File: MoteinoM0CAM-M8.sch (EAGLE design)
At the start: 17 parts

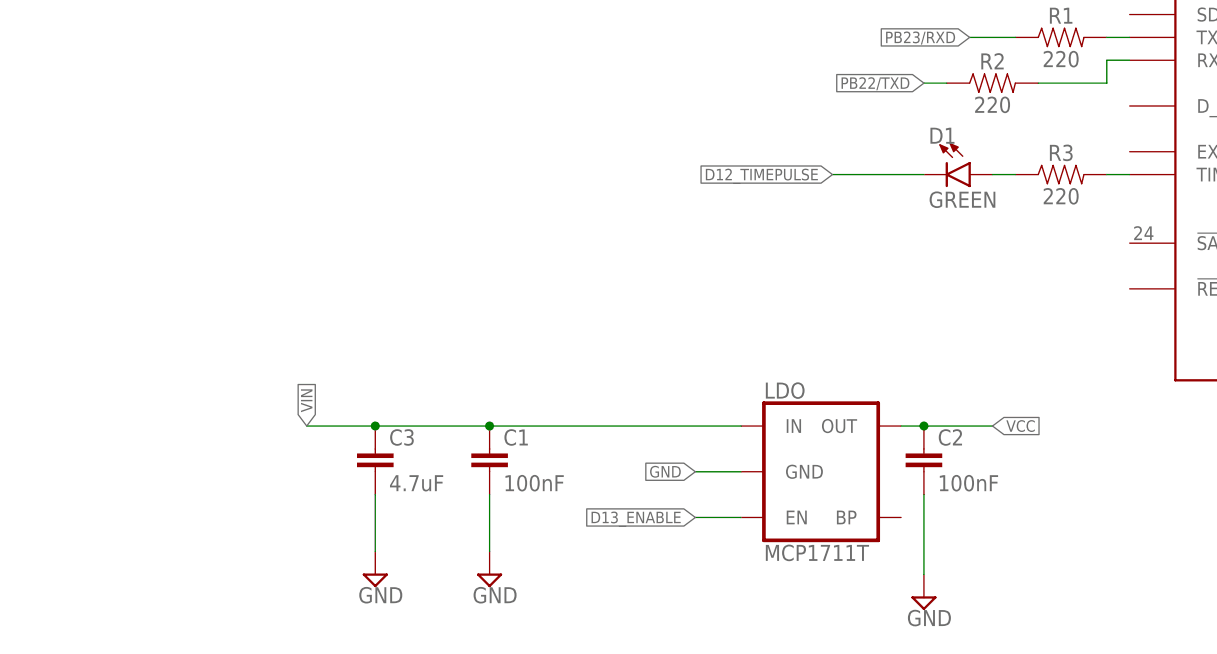
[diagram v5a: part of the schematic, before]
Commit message: moved 4.7uF
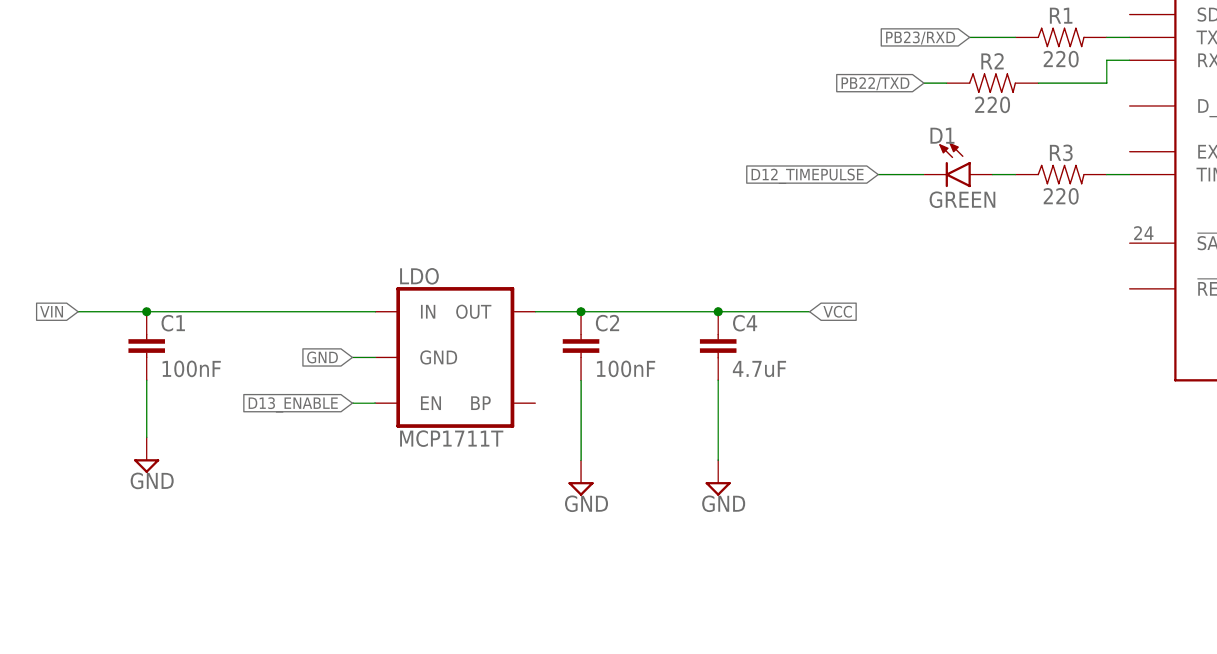
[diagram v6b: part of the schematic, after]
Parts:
- removed C3: 4.7uF, SparkFun-Capacitors:4.7UF0603
- added C4: 4.7uF, SparkFun-Capacitors:4.7UF0603
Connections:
- net GND: now also C4.2; no longer C3.2
- net VCC: now also C4.1
- net VIN: no longer C3.1
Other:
- moved on the sheet: C1, C2, LDO
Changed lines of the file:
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@@
 <part name="R2" library="SparkFun-Resistors" library_urn="urn:adsk.eagle:library:532" deviceset="220OHM" device="-0603-1/10W-1%" package3d_urn="urn:adsk.eagle:package:39650/1" value="220"/>
 <part name="R3" library="SparkFun-Resistors" library_urn="urn:adsk.eagle:library:532" deviceset="220OHM" device="-0603-1/10W-1%" package3d_urn="urn:adsk.eagle:package:39650/1" value="220"/>
-<part name="C3" library="SparkFun-Capacitors" library_urn="urn:adsk.eagle:library:510" deviceset="4.7UF" device="0603" package3d_urn="urn:adsk.eagle:package:37414/1" value="4.7uF"/>
-<part name="SUPPLY4" library="supply2" library_urn="urn:adsk.eagle:library:372" deviceset="GND" device=""/>
+<part name="C4" library="SparkFun-Capacitors" library_urn="urn:adsk.eagle:library:510" deviceset="4.7UF" device="0603" package3d_urn="urn:adsk.eagle:package:37414/1" value="4.7uF"/>
+<part name="SUPPLY5" library="supply2" library_urn="urn:adsk.eagle:library:372" deviceset="GND" device=""/>
 </parts>
 <sheets>
@@
 <attribute name="VALUE" x="47.752" y="162.814" size="1.778" layer="96" font="vector"/>
 </instance>
-<instance part="LDO" gate="G$1" x="55.88" y="106.68" smashed="yes">
-<attribute name="NAME" x="48.26" y="114.808" size="1.778" layer="95" font="vector"/>
-<attribute name="VALUE" x="48.26" y="98.552" size="1.778" layer="96" font="vector" align="top-left"/>
-</instance>
-<instance part="C1" gate="G$1" x="17.78" y="106.68" smashed="yes">
-<attribute name="NAME" x="19.304" y="109.601" size="1.778" layer="95" font="vector"/>
-<attribute name="VALUE" x="19.304" y="104.521" size="1.778" layer="96" font="vector"/>
-</instance>
-<instance part="C2" gate="G$1" x="66.04" y="106.68" smashed="yes">
-<attribute name="NAME" x="67.564" y="109.601" size="1.778" layer="95" font="vector"/>
-<attribute name="VALUE" x="67.564" y="104.521" size="1.778" layer="96" font="vector"/>
-</instance>
-<instance part="SUPPLY2" gate="GND" x="17.78" y="95.25" smashed="yes">
-<attribute name="VALUE" x="15.875" y="92.075" size="1.778" layer="96"/>
-</instance>
-<instance part="SUPPLY3" gate="GND" x="66.04" y="92.71" smashed="yes">
-<attribute name="VALUE" x="64.135" y="89.535" size="1.778" layer="96"/>
+<instance part="LDO" gate="G$1" x="15.24" y="119.38" smashed="yes">
+<attribute name="NAME" x="7.62" y="127.508" size="1.778" layer="95" font="vector"/>
+<attribute name="VALUE" x="7.62" y="111.252" size="1.778" layer="96" font="vector" align="top-left"/>
+</instance>
+<instance part="C1" gate="G$1" x="-20.32" y="119.38" smashed="yes">
+<attribute name="NAME" x="-18.796" y="122.301" size="1.778" layer="95" font="vector"/>
+<attribute name="VALUE" x="-18.796" y="117.221" size="1.778" layer="96" font="vector"/>
+</instance>
+<instance part="C2" gate="G$1" x="27.94" y="119.38" smashed="yes">
+<attribute name="NAME" x="29.464" y="122.301" size="1.778" layer="95" font="vector"/>
+<attribute name="VALUE" x="29.464" y="117.221" size="1.778" layer="96" font="vector"/>
+</instance>
+<instance part="SUPPLY2" gate="GND" x="-20.32" y="107.95" smashed="yes">
+<attribute name="VALUE" x="-22.225" y="104.775" size="1.778" layer="96"/>
+</instance>
+<instance part="SUPPLY3" gate="GND" x="27.94" y="105.41" smashed="yes">
+<attribute name="VALUE" x="26.035" y="102.235" size="1.778" layer="96"/>
 </instance>
 <instance part="SUPPLY1" gate="GND" x="15.24" y="173.99" smashed="yes">
@@
 <attribute name="VALUE" x="81.28" y="138.176" size="1.778" layer="96" font="vector" align="top-center"/>
 </instance>
-<instance part="C3" gate="G$1" x="5.08" y="106.68" smashed="yes">
-<attribute name="NAME" x="6.604" y="109.601" size="1.778" layer="95" font="vector"/>
-<attribute name="VALUE" x="6.604" y="104.521" size="1.778" layer="96" font="vector"/>
-</instance>
-<instance part="SUPPLY4" gate="GND" x="5.08" y="95.25" smashed="yes">
-<attribute name="VALUE" x="3.175" y="92.075" size="1.778" layer="96"/>
+<instance part="C4" gate="G$1" x="43.18" y="119.38" smashed="yes">
+<attribute name="NAME" x="44.704" y="122.301" size="1.778" layer="95" font="vector"/>
+<attribute name="VALUE" x="44.704" y="117.221" size="1.778" layer="96" font="vector"/>
+</instance>
+<instance part="SUPPLY5" gate="GND" x="43.18" y="105.41" smashed="yes">
+<attribute name="VALUE" x="41.275" y="102.235" size="1.778" layer="96"/>
 </instance>
 </instances>
@@
 <segment>
 <pinref part="LDO" gate="G$1" pin="GND"/>
-<wire x1="45.72" y1="106.68" x2="40.64" y2="106.68" width="0.1524" layer="91"/>
-<label x="40.64" y="106.68" size="1.27" layer="95" rot="R180" xref="yes"/>
+<wire x1="5.08" y1="119.38" x2="2.54" y2="119.38" width="0.1524" layer="91"/>
+<label x="2.54" y="119.38" size="1.27" layer="95" rot="R180" xref="yes"/>
 </segment>
 <segment>
 <pinref part="C1" gate="G$1" pin="2"/>
 <pinref part="SUPPLY2" gate="GND" pin="GND"/>
-<wire x1="17.78" y1="104.14" x2="17.78" y2="97.79" width="0.1524" layer="91"/>
+<wire x1="-20.32" y1="116.84" x2="-20.32" y2="110.49" width="0.1524" layer="91"/>
 </segment>
 <segment>
 <pinref part="SUPPLY3" gate="GND" pin="GND"/>
 <pinref part="C2" gate="G$1" pin="2"/>
-<wire x1="66.04" y1="104.14" x2="66.04" y2="95.25" width="0.1524" layer="91"/>
+<wire x1="27.94" y1="116.84" x2="27.94" y2="107.95" width="0.1524" layer="91"/>
 </segment>
 <segment>
@@
 </segment>
 <segment>
-<pinref part="C3" gate="G$1" pin="2"/>
-<wire x1="5.08" y1="104.14" x2="5.08" y2="97.79" width="0.1524" layer="91"/>
-<pinref part="SUPPLY4" gate="GND" pin="GND"/>
+<pinref part="C4" gate="G$1" pin="2"/>
+<pinref part="SUPPLY5" gate="GND" pin="GND"/>
+<wire x1="43.18" y1="116.84" x2="43.18" y2="107.95" width="0.1524" layer="91"/>
 </segment>
 </net>
@@
 <pinref part="LDO" gate="G$1" pin="IN"/>
 <pinref part="C1" gate="G$1" pin="1"/>
-<wire x1="45.72" y1="111.76" x2="17.78" y2="111.76" width="0.1524" layer="91"/>
-<wire x1="17.78" y1="111.76" x2="5.08" y2="111.76" width="0.1524" layer="91"/>
-<junction x="17.78" y="111.76"/>
-<label x="-2.54" y="111.76" size="1.27" layer="95" rot="R90" xref="yes"/>
-<pinref part="C3" gate="G$1" pin="1"/>
-<wire x1="5.08" y1="111.76" x2="-2.54" y2="111.76" width="0.1524" layer="91"/>
-<junction x="5.08" y="111.76"/>
+<wire x1="5.08" y1="124.46" x2="-20.32" y2="124.46" width="0.1524" layer="91"/>
+<wire x1="-20.32" y1="124.46" x2="-27.94" y2="124.46" width="0.1524" layer="91"/>
+<junction x="-20.32" y="124.46"/>
+<label x="-27.94" y="124.46" size="1.27" layer="95" rot="R180" xref="yes"/>
 </segment>
 </net>
@@
 <segment>
 <pinref part="D1" gate="G$1" pin="C"/>
-<wire x1="66.04" y1="139.7" x2="55.88" y2="139.7" width="0.1524" layer="91"/>
-<label x="55.88" y="139.7" size="1.27" layer="95" rot="R180" xref="yes"/>
+<wire x1="66.04" y1="139.7" x2="60.96" y2="139.7" width="0.1524" layer="91"/>
+<label x="60.96" y="139.7" size="1.27" layer="95" rot="R180" xref="yes"/>
 </segment>
 </net>
@@
 <segment>
 <pinref part="LDO" gate="G$1" pin="EN"/>
-<wire x1="45.72" y1="101.6" x2="40.64" y2="101.6" width="0.1524" layer="91"/>
-<label x="40.64" y="101.6" size="1.27" layer="95" rot="R180" xref="yes"/>
+<wire x1="5.08" y1="114.3" x2="2.54" y2="114.3" width="0.1524" layer="91"/>
+<label x="2.54" y="114.3" size="1.27" layer="95" rot="R180" xref="yes"/>
 </segment>
 <segment>
@@
 <pinref part="C2" gate="G$1" pin="1"/>
 <pinref part="LDO" gate="G$1" pin="OUT"/>
-<wire x1="63.5" y1="111.76" x2="66.04" y2="111.76" width="0.1524" layer="91"/>
-<junction x="66.04" y="111.76"/>
-<wire x1="66.04" y1="111.76" x2="73.66" y2="111.76" width="0.1524" layer="91"/>
-<label x="73.66" y="111.76" size="1.27" layer="95" xref="yes"/>
-</segment>
-</net>
+<wire x1="22.86" y1="124.46" x2="27.94" y2="124.46" width="0.1524" layer="91"/>
+<junction x="27.94" y="124.46"/>
+<wire x1="27.94" y1="124.46" x2="43.18" y2="124.46" width="0.1524" layer="91"/>
+<label x="53.34" y="124.46" size="1.27" layer="95" xref="yes"/>
+<pinref part="C4" gate="G$1" pin="1"/>
+<wire x1="43.18" y1="124.46" x2="53.34" y2="124.46" width="0.1524" layer="91"/>
+<junction x="43.18" y="124.46"/>
+</segment>
+</net>

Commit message: final
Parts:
- renumbered C4 to C3
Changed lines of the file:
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@@
 <part name="R2" library="SparkFun-Resistors" library_urn="urn:adsk.eagle:library:532" deviceset="220OHM" device="-0603-1/10W-1%" package3d_urn="urn:adsk.eagle:package:39650/1" value="220"/>
 <part name="R3" library="SparkFun-Resistors" library_urn="urn:adsk.eagle:library:532" deviceset="220OHM" device="-0603-1/10W-1%" package3d_urn="urn:adsk.eagle:package:39650/1" value="220"/>
-<part name="C4" library="SparkFun-Capacitors" library_urn="urn:adsk.eagle:library:510" deviceset="4.7UF" device="0603" package3d_urn="urn:adsk.eagle:package:37414/1" value="4.7uF"/>
+<part name="C3" library="SparkFun-Capacitors" library_urn="urn:adsk.eagle:library:510" deviceset="4.7UF" device="0603" package3d_urn="urn:adsk.eagle:package:37414/1" value="4.7uF"/>
 <part name="SUPPLY5" library="supply2" library_urn="urn:adsk.eagle:library:372" deviceset="GND" device=""/>
 </parts>
@@
 <attribute name="VALUE" x="81.28" y="138.176" size="1.778" layer="96" font="vector" align="top-center"/>
 </instance>
-<instance part="C4" gate="G$1" x="43.18" y="119.38" smashed="yes">
+<instance part="C3" gate="G$1" x="43.18" y="119.38" smashed="yes">
 <attribute name="NAME" x="44.704" y="122.301" size="1.778" layer="95" font="vector"/>
 <attribute name="VALUE" x="44.704" y="117.221" size="1.778" layer="96" font="vector"/>
@@
 </segment>
 <segment>
-<pinref part="C4" gate="G$1" pin="2"/>
+<pinref part="C3" gate="G$1" pin="2"/>
 <pinref part="SUPPLY5" gate="GND" pin="GND"/>
 <wire x1="43.18" y1="116.84" x2="43.18" y2="107.95" width="0.1524" layer="91"/>
@@
 <wire x1="27.94" y1="124.46" x2="43.18" y2="124.46" width="0.1524" layer="91"/>
 <label x="53.34" y="124.46" size="1.27" layer="95" xref="yes"/>
-<pinref part="C4" gate="G$1" pin="1"/>
+<pinref part="C3" gate="G$1" pin="1"/>
 <wire x1="43.18" y1="124.46" x2="53.34" y2="124.46" width="0.1524" layer="91"/>
 <junction x="43.18" y="124.46"/>

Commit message: Corrected 1203 to 0603 LED
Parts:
- D1: device SparkFun-LED:LED-GREEN1206 -> SparkFun-LED:LED-GREEN0603
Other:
- note added: "R2"
- note removed: "R1"
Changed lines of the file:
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@@
 <part name="SUPPLY3" library="supply2" library_urn="urn:adsk.eagle:library:372" deviceset="GND" device=""/>
 <part name="SUPPLY1" library="supply2" library_urn="urn:adsk.eagle:library:372" deviceset="GND" device=""/>
-<part name="D1" library="SparkFun-LED" library_urn="urn:adsk.eagle:library:529" deviceset="LED-GREEN" device="1206" package3d_urn="urn:adsk.eagle:package:39352/1" value="GREEN"/>
 <part name="R1" library="SparkFun-Resistors" library_urn="urn:adsk.eagle:library:532" deviceset="220OHM" device="-0603-1/10W-1%" package3d_urn="urn:adsk.eagle:package:39650/1" value="220"/>
 <part name="R2" library="SparkFun-Resistors" library_urn="urn:adsk.eagle:library:532" deviceset="220OHM" device="-0603-1/10W-1%" package3d_urn="urn:adsk.eagle:package:39650/1" value="220"/>
@@
 <part name="C3" library="SparkFun-Capacitors" library_urn="urn:adsk.eagle:library:510" deviceset="4.7UF" device="0603" package3d_urn="urn:adsk.eagle:package:37414/1" value="4.7uF"/>
 <part name="SUPPLY5" library="supply2" library_urn="urn:adsk.eagle:library:372" deviceset="GND" device=""/>
+<part name="D1" library="SparkFun-LED" library_urn="urn:adsk.eagle:library:529" deviceset="LED-GREEN" device="0603" package3d_urn="urn:adsk.eagle:package:39354/1" value="GREEN"/>
 </parts>
 <sheets>
@@
 <plain>
 <text x="27.94" y="203.2" size="3.048" layer="94" ratio="12">Greg Cope</text>
-<text x="138.43" y="203.2" size="3.048" layer="94" ratio="12">R1</text>
+<text x="138.43" y="203.2" size="3.048" layer="94" ratio="12">R2</text>
 <text x="27.94" y="208.28" size="4.572" layer="94" ratio="15">MoteinoM0 CAM-M8Q Breakout</text>
 </plain>
@@
 <attribute name="VALUE" x="13.335" y="170.815" size="1.778" layer="96"/>
 </instance>
+<instance part="R1" gate="G$1" x="81.28" y="154.94" smashed="yes">
+<attribute name="NAME" x="81.28" y="156.464" size="1.778" layer="95" font="vector" align="bottom-center"/>
+<attribute name="VALUE" x="81.28" y="153.416" size="1.778" layer="96" font="vector" align="top-center"/>
+</instance>
+<instance part="R2" gate="G$1" x="73.66" y="149.86" smashed="yes">
+<attribute name="NAME" x="73.66" y="151.384" size="1.778" layer="95" font="vector" align="bottom-center"/>
+<attribute name="VALUE" x="73.66" y="148.336" size="1.778" layer="96" font="vector" align="top-center"/>
+</instance>
+<instance part="R3" gate="G$1" x="81.28" y="139.7" smashed="yes">
+<attribute name="NAME" x="81.28" y="141.224" size="1.778" layer="95" font="vector" align="bottom-center"/>
+<attribute name="VALUE" x="81.28" y="138.176" size="1.778" layer="96" font="vector" align="top-center"/>
+</instance>
+<instance part="C3" gate="G$1" x="43.18" y="119.38" smashed="yes">
+<attribute name="NAME" x="44.704" y="122.301" size="1.778" layer="95" font="vector"/>
+<attribute name="VALUE" x="44.704" y="117.221" size="1.778" layer="96" font="vector"/>
+</instance>
+<instance part="SUPPLY5" gate="GND" x="43.18" y="105.41" smashed="yes">
+<attribute name="VALUE" x="41.275" y="102.235" size="1.778" layer="96"/>
+</instance>
 <instance part="D1" gate="G$1" x="71.12" y="139.7" smashed="yes" rot="R270">
 <attribute name="NAME" x="66.548" y="143.129" size="1.778" layer="95" font="vector"/>
 <attribute name="VALUE" x="66.548" y="137.795" size="1.778" layer="96" font="vector" align="top-left"/>
-</instance>
-<instance part="R1" gate="G$1" x="81.28" y="154.94" smashed="yes">
-<attribute name="NAME" x="81.28" y="156.464" size="1.778" layer="95" font="vector" align="bottom-center"/>
-<attribute name="VALUE" x="81.28" y="153.416" size="1.778" layer="96" font="vector" align="top-center"/>
-</instance>
-<instance part="R2" gate="G$1" x="73.66" y="149.86" smashed="yes">
-<attribute name="NAME" x="73.66" y="151.384" size="1.778" layer="95" font="vector" align="bottom-center"/>
-<attribute name="VALUE" x="73.66" y="148.336" size="1.778" layer="96" font="vector" align="top-center"/>
-</instance>
-<instance part="R3" gate="G$1" x="81.28" y="139.7" smashed="yes">
-<attribute name="NAME" x="81.28" y="141.224" size="1.778" layer="95" font="vector" align="bottom-center"/>
-<attribute name="VALUE" x="81.28" y="138.176" size="1.778" layer="96" font="vector" align="top-center"/>
-</instance>
-<instance part="C3" gate="G$1" x="43.18" y="119.38" smashed="yes">
-<attribute name="NAME" x="44.704" y="122.301" size="1.778" layer="95" font="vector"/>
-<attribute name="VALUE" x="44.704" y="117.221" size="1.778" layer="96" font="vector"/>
-</instance>
-<instance part="SUPPLY5" gate="GND" x="43.18" y="105.41" smashed="yes">
-<attribute name="VALUE" x="41.275" y="102.235" size="1.778" layer="96"/>
 </instance>
 </instances>
@@
 </segment>
 <segment>
-<pinref part="D1" gate="G$1" pin="C"/>
 <wire x1="66.04" y1="139.7" x2="60.96" y2="139.7" width="0.1524" layer="91"/>
 <label x="60.96" y="139.7" size="1.27" layer="95" rot="R180" xref="yes"/>
+<pinref part="D1" gate="G$1" pin="C"/>
 </segment>
 </net>
@@
 <segment>
 <pinref part="R3" gate="G$1" pin="1"/>
+<wire x1="76.2" y1="139.7" x2="73.66" y2="139.7" width="0.1524" layer="91"/>
 <pinref part="D1" gate="G$1" pin="A"/>
-<wire x1="76.2" y1="139.7" x2="73.66" y2="139.7" width="0.1524" layer="91"/>
-</segment>
-</net>
+</segment>
+</net>
